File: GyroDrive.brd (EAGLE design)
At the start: 10.7 x 19.8 mm, 55 parts, among them IC1 AD8235, IC2 AD8235, IC3 AD8235, IC4 AD8235

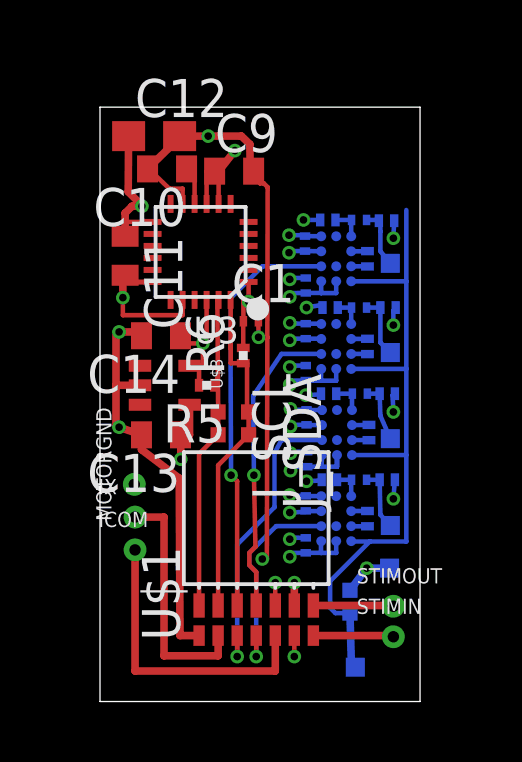
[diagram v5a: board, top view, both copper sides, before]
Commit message: Added high pass filter for VGND. Attachment point for AGND changed to through hole.
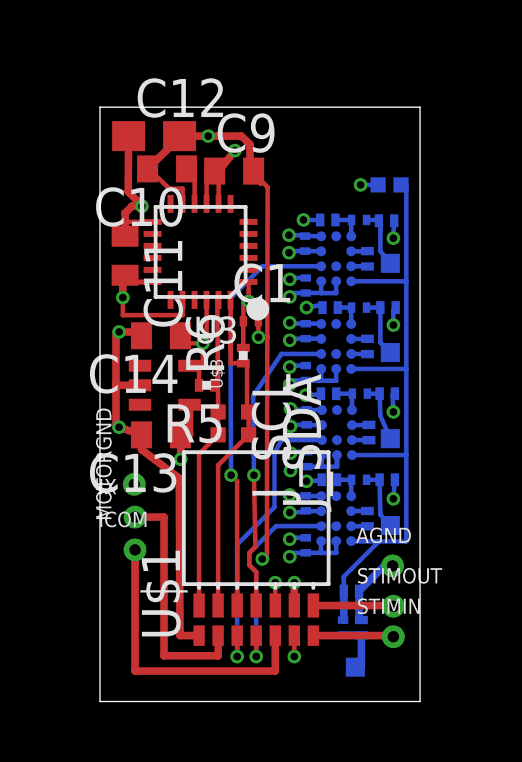
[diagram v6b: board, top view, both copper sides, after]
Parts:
- added C6: (no value), resistor:C0201
- added R15, R16: (no value), resistor:R0201
- AGND: device michael-stetner:SMD25-25-MIL -> michael-stetner:30MIL/15MIL
- moved J_VGND 14.0 mm to (9.65, 17.2), turned to 0 degrees
- moved AGND 0.13 mm to (9.75, 4.52), flipped to the top
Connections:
- new net VGND_IN: C6.1, R15.2, VGND.1
- net AGND: now also AGND.P$1, R15.1, R16.1; no longer AGND.1
- net VGND: now also C6.2, R16.2; no longer VGND.1
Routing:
- net VGND_IN: track 0.00 -> 1.88 mm
- net AGND: track 14.2 -> 15.7 mm
- net VGND: track 23.8 -> 22.5 mm
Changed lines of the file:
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@@
 <layers>
 <layer number="1" name="Top" color="4" fill="1" visible="yes" active="yes"/>
-<layer number="2" name="Route2" color="13" fill="3" visible="yes" active="yes"/>
+<layer number="2" name="Route2" color="13" fill="3" visible="no" active="yes"/>
 <layer number="3" name="Route3" color="4" fill="3" visible="no" active="no"/>
 <layer number="14" name="Route14" color="1" fill="6" visible="no" active="no"/>
@@
 <element name="R9" library="resistor" package="R0201" value="" x="8.9662" y="8.9662" rot="MR270"/>
 <element name="R10" library="resistor" package="R0201" value="" x="8.9154" y="6.096" rot="MR270"/>
-<element name="J_VGND" library="michael-stetner" package="SJ" value="" x="8.3312" y="3.3274" rot="MR90"/>
+<element name="J_VGND" library="michael-stetner" package="SJ" value="" x="9.652" y="17.2212" rot="MR0"/>
 <element name="E2" library="michael-stetner" package="SMD25-25-MIL" value="" x="9.6774" y="11.6332" rot="MR0"/>
 <element name="E3" library="michael-stetner" package="SMD25-25-MIL" value="" x="9.6774" y="8.763" rot="MR0"/>
 <element name="E4" library="michael-stetner" package="SMD25-25-MIL" value="" x="9.6774" y="5.8674" rot="MR0"/>
 <element name="VGND" library="michael-stetner" package="SMD25-25-MIL" value="" x="8.509" y="1.143" rot="MR0"/>
-<element name="AGND" library="michael-stetner" package="SMD25-25-MIL" value="" x="9.652" y="4.445" rot="MR0"/>
 <element name="E1" library="michael-stetner" package="SMD25-25-MIL" value="" x="9.6774" y="14.605" rot="MR0"/>
 <element name="C1" library="resistor" package="C0201" value="" x="5.0292" y="12.6746"/>
@@
 <element name="C5" library="resistor" package="C0201" value="" x="8.636" y="7.3914" rot="MR0"/>
 <element name="R14" library="resistor" package="R0201" value="" x="7.6454" y="7.3914" rot="MR180"/>
+<element name="R15" library="resistor" package="R0201" value="" x="8.7122" y="2.4638" rot="MR270"/>
+<element name="C6" library="resistor" package="C0201" value="" x="8.1026" y="2.4638" rot="MR90"/>
+<element name="R16" library="resistor" package="R0201" value="" x="8.382" y="3.683" rot="MR0"/>
+<element name="AGND" library="michael-stetner" package="30MIL/15MIL" value="" x="9.7536" y="4.5212"/>
 </elements>
 <signals>
@@
 <wire x1="5.207" y1="3.9624" x2="5.207" y2="3.81" width="0.254" layer="15"/>
 <contactref element="MOTORGND" pad="P$1"/>
-<contactref element="AGND" pad="1"/>
-<wire x1="8.89" y1="4.445" x2="9.652" y2="4.445" width="0.254" layer="16"/>
-<wire x1="8.3312" y1="3.7084" x2="8.89" y2="4.445" width="0.254" layer="16"/>
-<via x="8.89" y="4.445" extent="1-16" drill="0.254"/>
 <contactref element="U$1" pad="D"/>
 <wire x1="6.477" y1="2.1971" x2="6.477" y2="1.4986" width="0.1524" layer="1"/>
@@
 <wire x1="7.3142" y1="13.208" x2="6.8834" y2="13.1318" width="0.1524" layer="16"/>
 <via x="6.8834" y="13.1318" extent="1-16" drill="0.254"/>
+<contactref element="R15" pad="1"/>
+<contactref element="R16" pad="1"/>
+<wire x1="8.7122" y1="2.7188" x2="8.637" y2="2.7188" width="0.254" layer="16"/>
+<wire x1="8.637" y1="2.7188" x2="8.637" y2="3.683" width="0.254" layer="16"/>
+<contactref element="AGND" pad="P$1"/>
+<wire x1="9.7536" y1="4.5212" x2="9.4752" y2="4.5212" width="0.254" layer="16"/>
+<wire x1="9.4752" y1="4.5212" x2="8.637" y2="3.683" width="0.254" layer="16"/>
+<wire x1="9.271" y1="17.2212" x2="8.6868" y2="17.2212" width="0.1524" layer="16"/>
+<via x="8.6868" y="17.2212" extent="1-16" drill="0.254"/>
+<wire x1="8.6868" y1="17.2212" x2="8.6868" y2="17.0942" width="0.1524" layer="15"/>
 </signal>
 <signal name="S1">
@@
 <contactref element="IC3" pad="A3"/>
 <contactref element="IC4" pad="A3"/>
-<wire x1="8.386" y1="5.334" x2="8.9916" y2="5.334" width="0.1524" layer="16"/>
-<wire x1="8.9916" y1="5.334" x2="10.2108" y2="5.334" width="0.1524" layer="16"/>
+<wire x1="8.386" y1="5.334" x2="9.2964" y2="5.334" width="0.1524" layer="16"/>
+<wire x1="9.2964" y1="5.334" x2="10.2108" y2="5.334" width="0.1524" layer="16"/>
 <wire x1="10.2108" y1="5.334" x2="10.2108" y2="8.2162" width="0.1524" layer="16"/>
 <wire x1="10.2108" y1="8.2162" x2="10.2108" y2="11.0864" width="0.1524" layer="16"/>
@@
 <wire x1="8.3994" y1="8.2162" x2="10.2108" y2="8.2162" width="0.1524" layer="16"/>
 <contactref element="J_VGND" pad="1"/>
-<contactref element="VGND" pad="1"/>
-<wire x1="8.3312" y1="2.9464" x2="8.382" y2="1.143" width="0.254" layer="16"/>
-<wire x1="8.382" y1="1.143" x2="8.509" y2="1.143" width="0.254" layer="16"/>
-<wire x1="8.3312" y1="2.9464" x2="7.8486" y2="2.9464" width="0.1524" layer="16"/>
-<wire x1="7.8486" y1="2.9464" x2="7.6708" y2="3.1242" width="0.1524" layer="16"/>
-<wire x1="7.6708" y1="3.1242" x2="7.6708" y2="4.0132" width="0.1524" layer="16"/>
-<wire x1="7.6708" y1="4.0132" x2="8.9916" y2="5.334" width="0.1524" layer="16"/>
 <wire x1="8.382" y1="5.338" x2="8.374" y2="5.346" width="0.1524" layer="16"/>
 <wire x1="8.386" y1="5.334" x2="8.374" y2="5.346" width="0.1524" layer="16"/>
-<wire x1="10.2108" y1="14.0074" x2="10.2108" y2="16.383" width="0.1524" layer="16"/>
+<wire x1="10.2108" y1="14.0074" x2="10.2108" y2="17.2212" width="0.1524" layer="16"/>
+<contactref element="R16" pad="2"/>
+<contactref element="C6" pad="2"/>
+<wire x1="8.1026" y1="2.7138" x2="8.127" y2="2.7138" width="0.254" layer="16"/>
+<wire x1="8.127" y1="2.7138" x2="8.127" y2="3.683" width="0.254" layer="16"/>
+<wire x1="8.127" y1="3.683" x2="8.127" y2="4.1646" width="0.1524" layer="16"/>
+<wire x1="8.127" y1="4.1646" x2="9.2964" y2="5.334" width="0.1524" layer="16"/>
+<wire x1="10.2108" y1="17.2212" x2="10.033" y2="17.2212" width="0.1524" layer="16"/>
 </signal>
 <signal name="S3">
@@
 <wire x1="8.4114" y1="10.2616" x2="7.875" y2="10.2616" width="0.1524" layer="16"/>
 </signal>
+<signal name="VGND_IN">
+<contactref element="VGND" pad="1"/>
+<contactref element="C6" pad="1"/>
+<contactref element="R15" pad="2"/>
+<wire x1="8.509" y1="1.143" x2="8.7122" y2="1.143" width="0.254" layer="16"/>
+<wire x1="8.7122" y1="1.143" x2="8.7122" y2="2.2088" width="0.254" layer="16"/>
+<wire x1="8.7122" y1="2.2088" x2="8.1026" y2="2.2088" width="0.254" layer="16"/>
+<wire x1="8.1026" y1="2.2088" x2="8.1026" y2="2.2138" width="0.254" layer="16"/>
+</signal>
 </signals>
